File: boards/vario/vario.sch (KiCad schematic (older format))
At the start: 26 parts, among them J1 Conn_02x20_Odd_Even, J2 SD_Card, J3 Mini-DIN-6, Q5 Q_NMOS_DSG, U34 74LS273, U35 74HC244, U36 IFX54441EJV33

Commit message: SPI: invert RDY
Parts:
- removed Q5: Q_NMOS_DSG, symbol Device:Q_NMOS_DSG
- added Q?: Q_NMOS_GSD, symbol Device:Q_NMOS_GSD
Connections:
- net GND: now also Q?.2 (S)
- net ~miso: now also Q?.3 (D)
- net at J2.7 (DAT0), R11.2: now also Q?.1 (G)
- net ~rdy renamed rdy
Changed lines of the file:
@@
 ~rst
 Text Label 1800 1850 2    50   ~ 0
-~rdy
+rdy
 Text Label 2300 1850 0    50   ~ 0
 ena
@@
 	4200 2150 5600 2150
 Text GLabel 1400 1850 0    50   3State ~ 0
-~rdy
+rdy
 Wire Wire Line
 	1400 1850 1800 1850
@@
 	8950 6250 8950 6300
 $Comp
-L Device:Q_NMOS_DSG Q5
-U 1 1 5FEDCEB8
-P 6000 7550
-F 0 "Q5" H 6205 7596 50  0000 L CNN
-F 1 "Q_NMOS_DSG" H 6205 7505 50  0000 L CNN
-F 2 "" H 6200 7650 50  0001 C CNN
-F 3 "~" H 6000 7550 50  0001 C CNN
-	1    6000 7550
-	-1   0    0    -1
-$EndComp
-$Comp
 L Device:R R9
 U 1 1 5FEE1EBB
@@
 Wire Wire Line
 	5500 6450 5250 6450
-Connection ~ 5900 7350
 Text Label 5350 6450 0    50   ~ 0
 ~miso
@@
 Wire Bus Line
 	4200 2150 4200 5750
+$Comp
+L Device:Q_NMOS_GSD Q?
+U 1 1 6021BDC6
+P 6000 7550
+F 0 "Q?" H 6205 7596 50  0000 L CNN
+F 1 "Q_NMOS_GSD" H 6205 7505 50  0000 L CNN
+F 2 "" H 6200 7650 50  0001 C CNN
+F 3 "~" H 6000 7550 50  0001 C CNN
+	1    6000 7550
+	-1   0    0    -1
+$EndComp
+Connection ~ 5900 7350
 $EndSCHEMATC

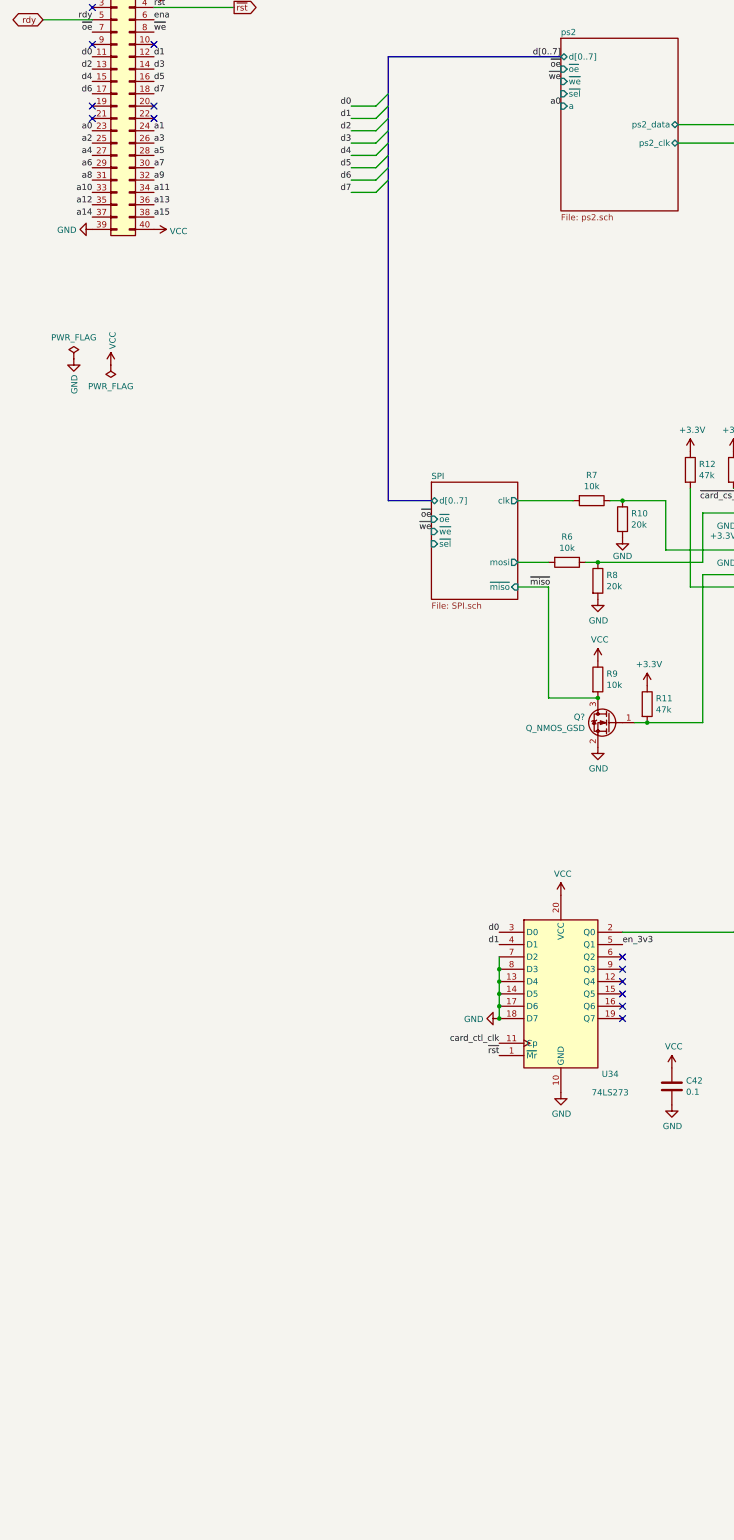
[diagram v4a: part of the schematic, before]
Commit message: PS/2: different select signals
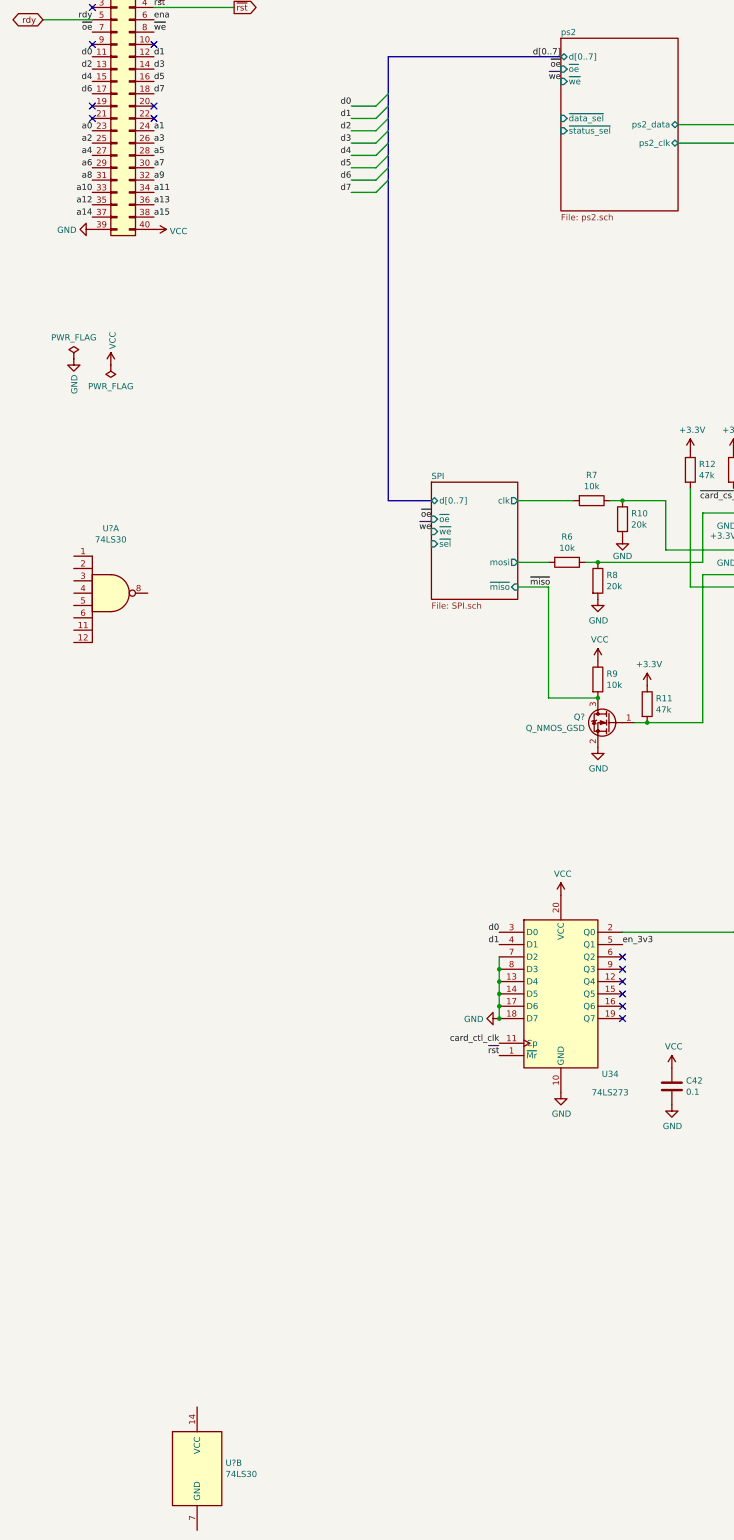
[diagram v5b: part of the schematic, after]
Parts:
- added U? (x2): 74LS30, symbol 74xx:74LS30
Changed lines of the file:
@@
 F5 "~oe" I L 5600 2250 50
 F6 "~we" I L 5600 2350 50
-F7 "~sel" I L 5600 2450 50
-F8 "a" I L 5600 2550 50
+F7 "~data_sel" I L 5600 2650 50
+F8 "~status_sel" I L 5600 2750 50
 $EndSheet
 Text GLabel 2950 1750 2    50   Output ~ 0
@@
 Text Label 5600 2350 2    50   ~ 0
 ~we
-Text Label 5600 2550 2    50   ~ 0
-a0
 Entry Wire Line
 	4100 2550 4200 2450
@@
 Wire Wire Line
 	9250 10150 9250 10250
-Wire Bus Line
-	4200 2150 4200 5750
 $Comp
 L Device:Q_NMOS_GSD Q?
@@
 $EndComp
 Connection ~ 5900 7350
+Wire Bus Line
+	4200 2150 4200 5750
+$Comp
+L 74xx:74LS30 U?
+U 1 1 6022739C
+P 1950 6500
+F 0 "U?" H 1950 7025 50  0000 C CNN
+F 1 "74LS30" H 1950 6934 50  0000 C CNN
+F 2 "" H 1950 6500 50  0001 C CNN
+F 3 "http://www.ti.com/lit/gpn/sn74LS30" H 1950 6500 50  0001 C CNN
+	1    1950 6500
+	1    0    0    -1
+$EndComp
+$Comp
+L 74xx:74LS30 U?
+U 2 1 602286DA
+P 2650 13600
+F 0 "U?" H 2880 13646 50  0000 L CNN
+F 1 "74LS30" H 2880 13555 50  0000 L CNN
+F 2 "" H 2650 13600 50  0001 C CNN
+F 3 "http://www.ti.com/lit/gpn/sn74LS30" H 2650 13600 50  0001 C CNN
+	2    2650 13600
+	1    0    0    -1
+$EndComp
 $EndSCHEMATC

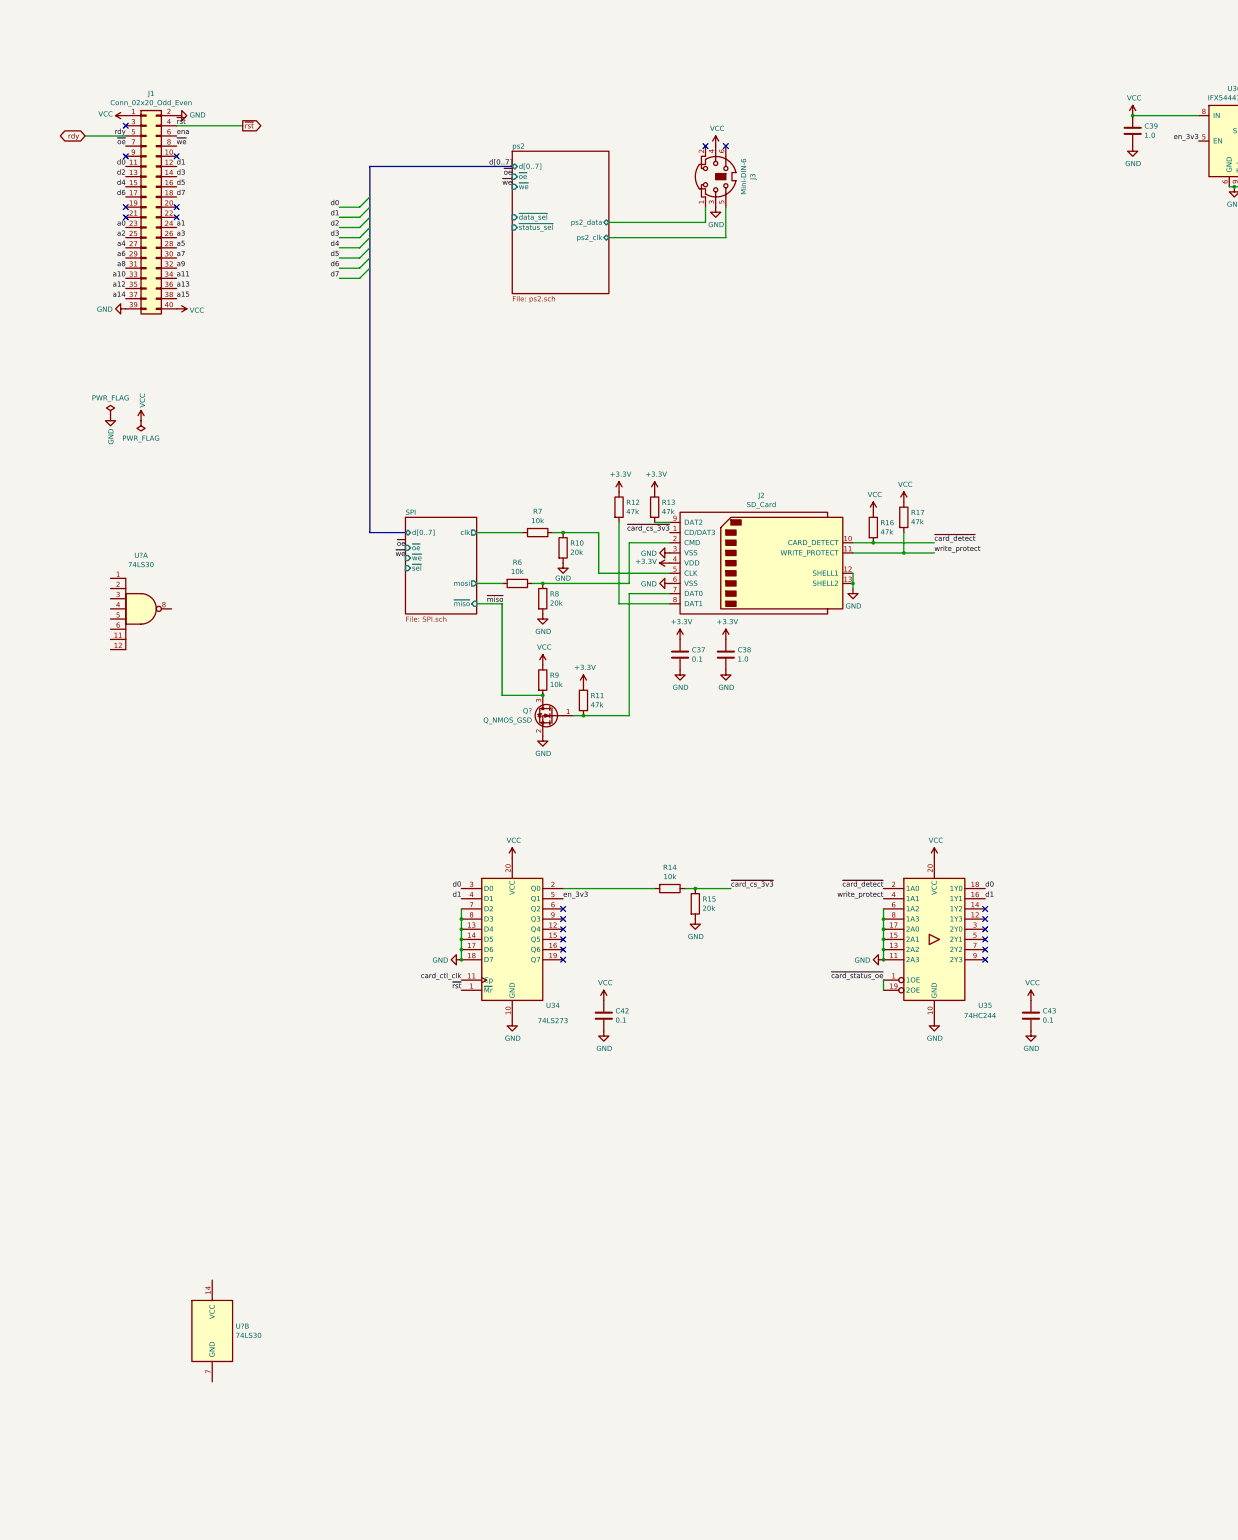
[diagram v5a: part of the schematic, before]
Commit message: Vario: address selection
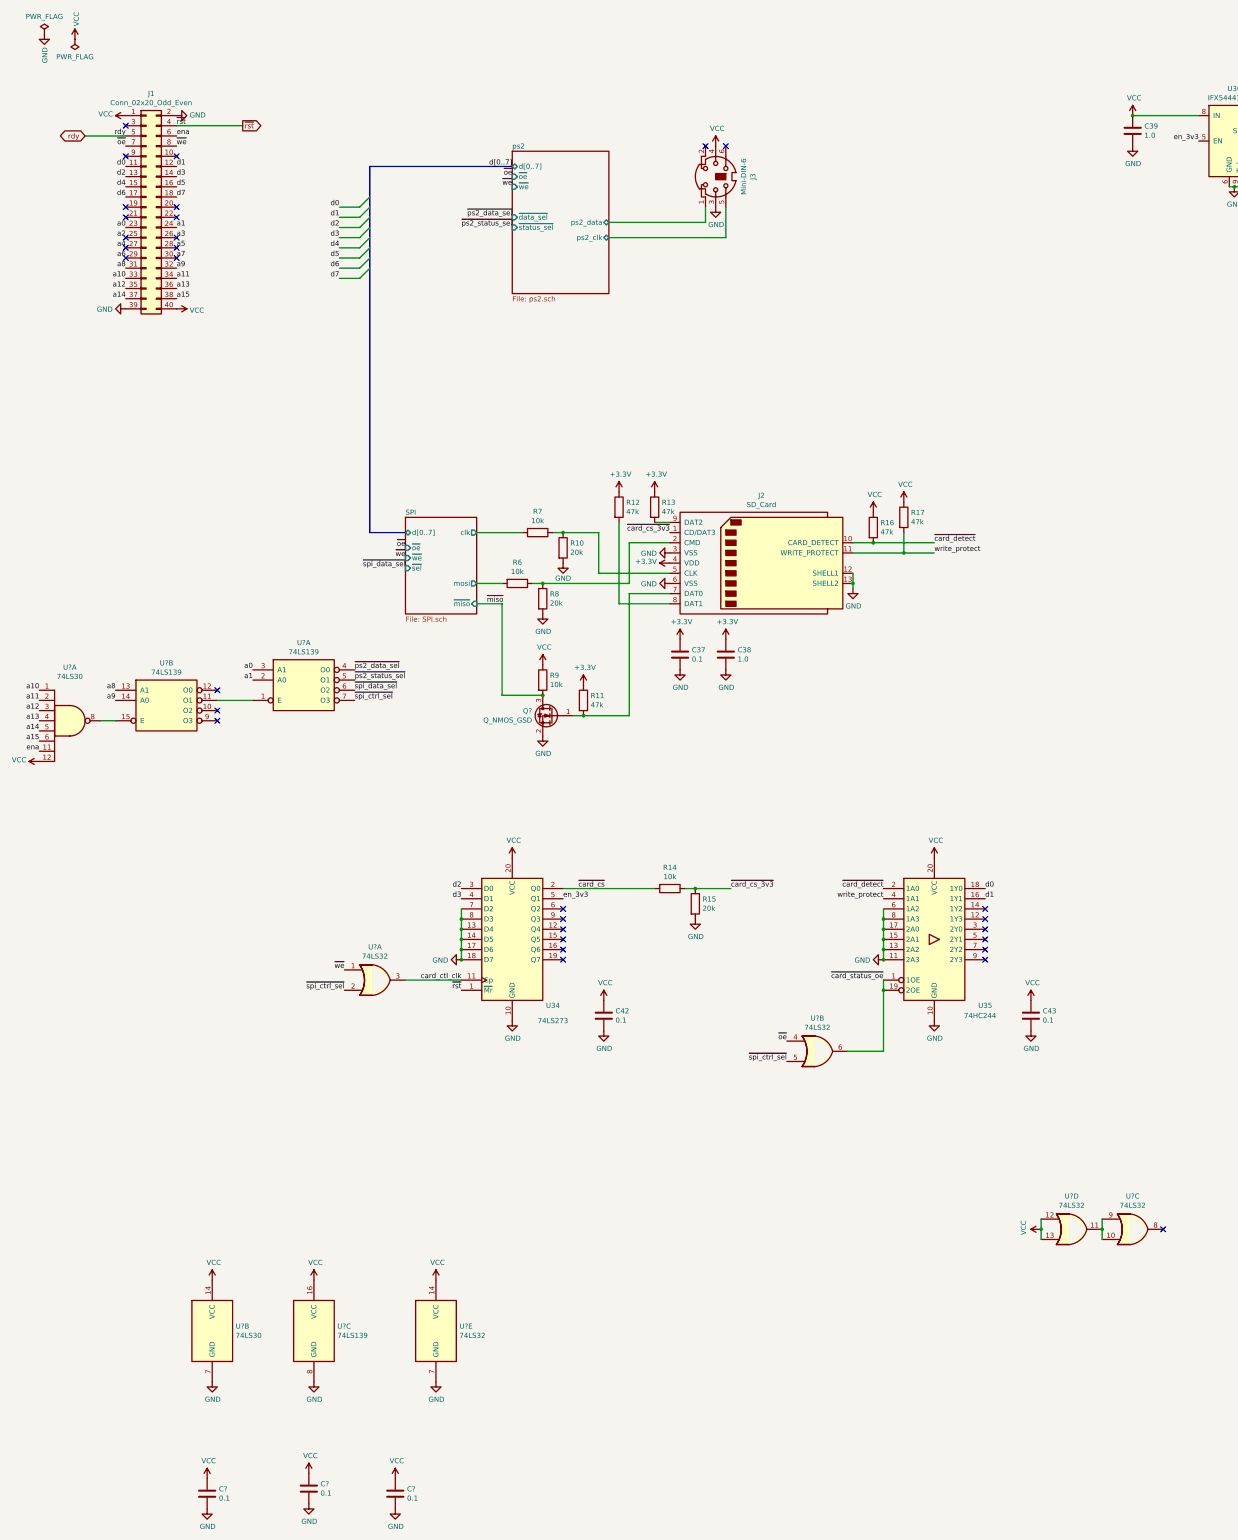
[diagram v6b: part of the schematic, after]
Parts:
- added C? (x3): 0.1, symbol Device:C
- added U? (x3): 74LS139, symbol 74xx:74LS139
- added U? (x5): 74LS32, symbol 74xx:74LS32
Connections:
- net GND: now also U?.7 (GND), C?.2, C?.2, C?.2, U?.7 (GND), U?.8 (GND)
- net VCC: now also U?.12, U?.14 (VCC), C?.1, C?.1, C?.1, U?.12, U?.13, U?.14 (VCC), U?.16 (VCC)
- net a0: now also U?.3 (A1)
- net a1: now also U?.2 (A0)
- net a10: now also U?.1
- net a11: now also U?.2
- net a12: now also U?.3
- net a13: now also U?.4
- net a14: now also U?.5
- net a15: now also U?.6
- net a8: now also U?.13 (A1)
- net a9: now also U?.14 (A0)
- net card_ctl_clk: now also U?.3
- net d0: no longer U34.3 (D0)
- net d1: no longer U34.4 (D1)
- net d2: now also U34.3 (D0)
- net d3: now also U34.4 (D1)
- net ena: now also U?.11
- net ~card_status_oe: now also U?.6
- net ~oe: now also U?.4
- net ~we: now also U?.1
- net ~card_cs: now reaches R14.2, U34.2 (Q0)
- net at U?.8: now also U?.15 (E)
- new net: U?.1 (E), U?.11 (O1)
- new net: U?.10, U?.11, U?.9
- new net ~ps2_data_sel: U?.4 (O0)
- new net ~ps2_status_sel: U?.5 (O1)
- new net ~spi_ctrl_sel: U?.2, U?.5, U?.7 (O3)
- new net ~spi_data_sel: U?.6 (O2)
- no-connect marks 21 -> 31
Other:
- moved on the sheet: U?A
